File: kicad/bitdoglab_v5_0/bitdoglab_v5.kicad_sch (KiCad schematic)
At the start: 45 parts, among them J1 Conn_01x20_Socket, J10 GND, J11 GND, J12 Conn_01x05_Pin, J13 Conn_01x05_Pin, J14 5x5 Matrix led, J15 GND, J16 GND, J17 GND, J18 GND, J19 JOYSTICK, J2 conector_idc, J3 Conn_01x20_Socket, J4 jumper_mic, J5 Conn_01x05_Pin, J6 Conn_01x05_Pin, J7 GND, J8 GND, J9 GND, Q1 DMG2305UX-13, Q2 BC337, Q3 BC337, SW1 RESET, SW2 Button_A, SW3 Button_B, U1 3.3v_tht, U2 LM1117DT-ADJ, U3 BAT (DIS)CHARGE, U4 1063

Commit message: inicio da sincronizacao do esquematico da versão 5.0
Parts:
- added V_BAT1: JST_EH_B2B-EH-A_1x02_P2.50mm_Vertical, symbol Connector:Screw_Terminal_01x02
- Charge DisCharge1: renamed from U3
- J10: value GND -> 3V3
- J11: value GND -> 5V-VSYS
- J15: value GND -> 0
- J16: value GND -> 1
- J17: value GND -> 2
- J18: value GND -> 3
- J8: value GND -> ANA-IN
- LED RGB1: renamed from D1
- Reg_3V3: renamed from U2; value LM1117DT-ADJ -> 3.3v_smd; footprint Package_TO_SOT_SMD:TO-252-3_TabPin2 -> Package_TO_SOT_SMD:SOT-223
- SW1: value RESET -> Reset
- SW2: value Button_A -> Botão
- U4: value 1063 -> MIC
- renumbered BZ2 to Buzzer1

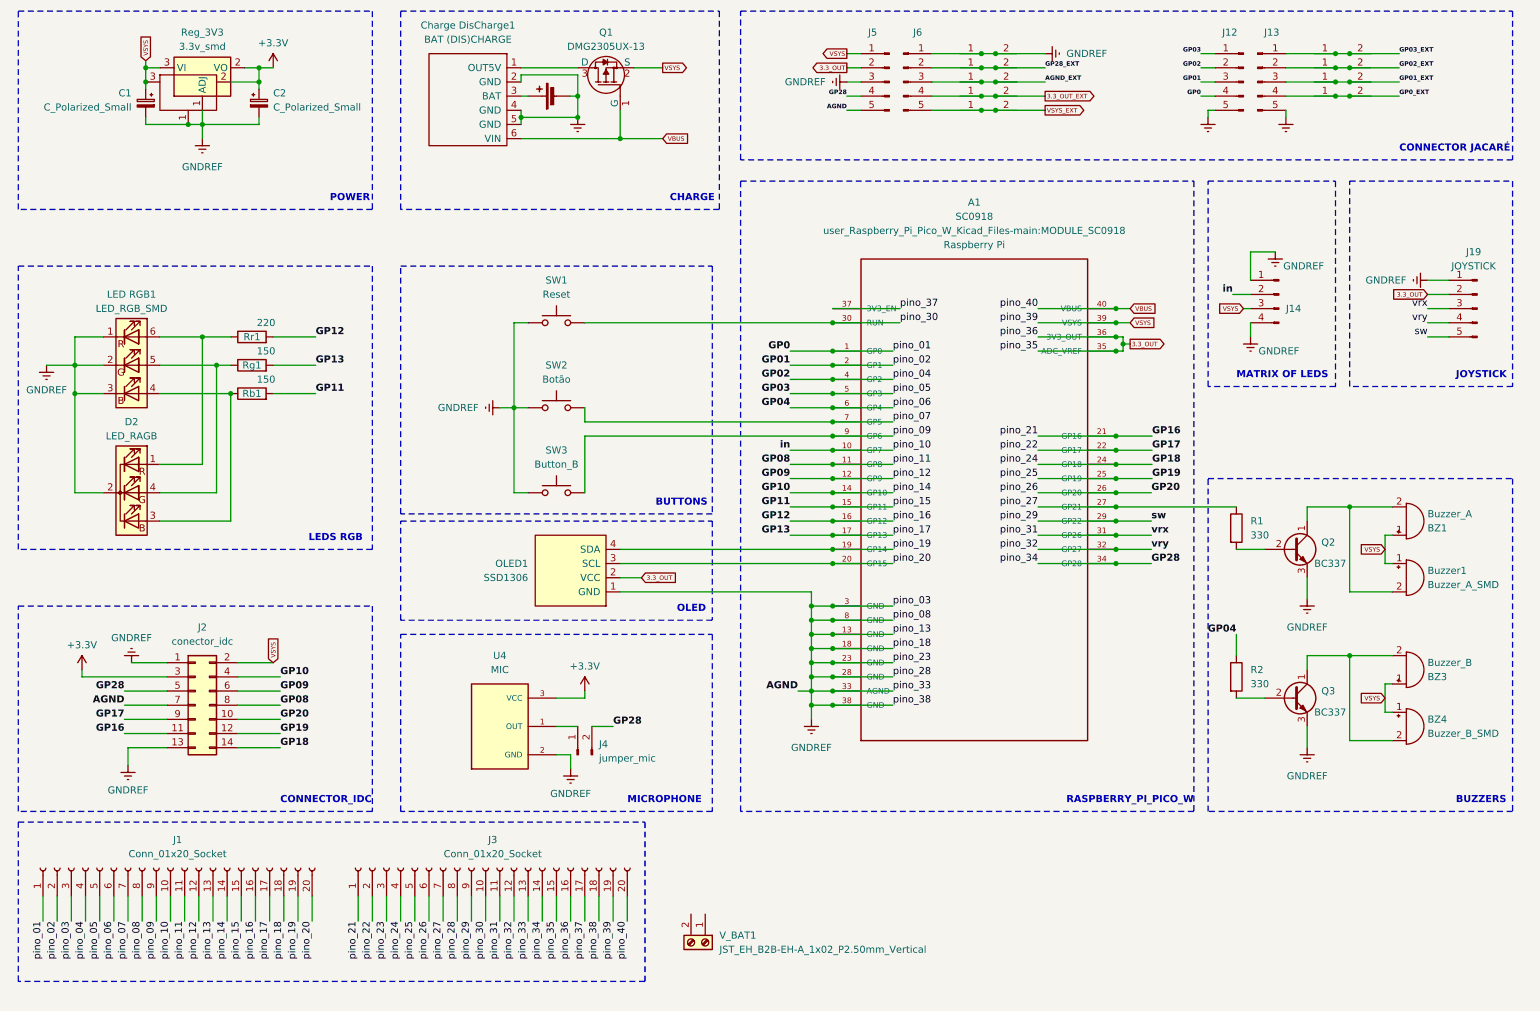
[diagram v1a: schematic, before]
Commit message: Sincronizar layout com esquematico - parte 1
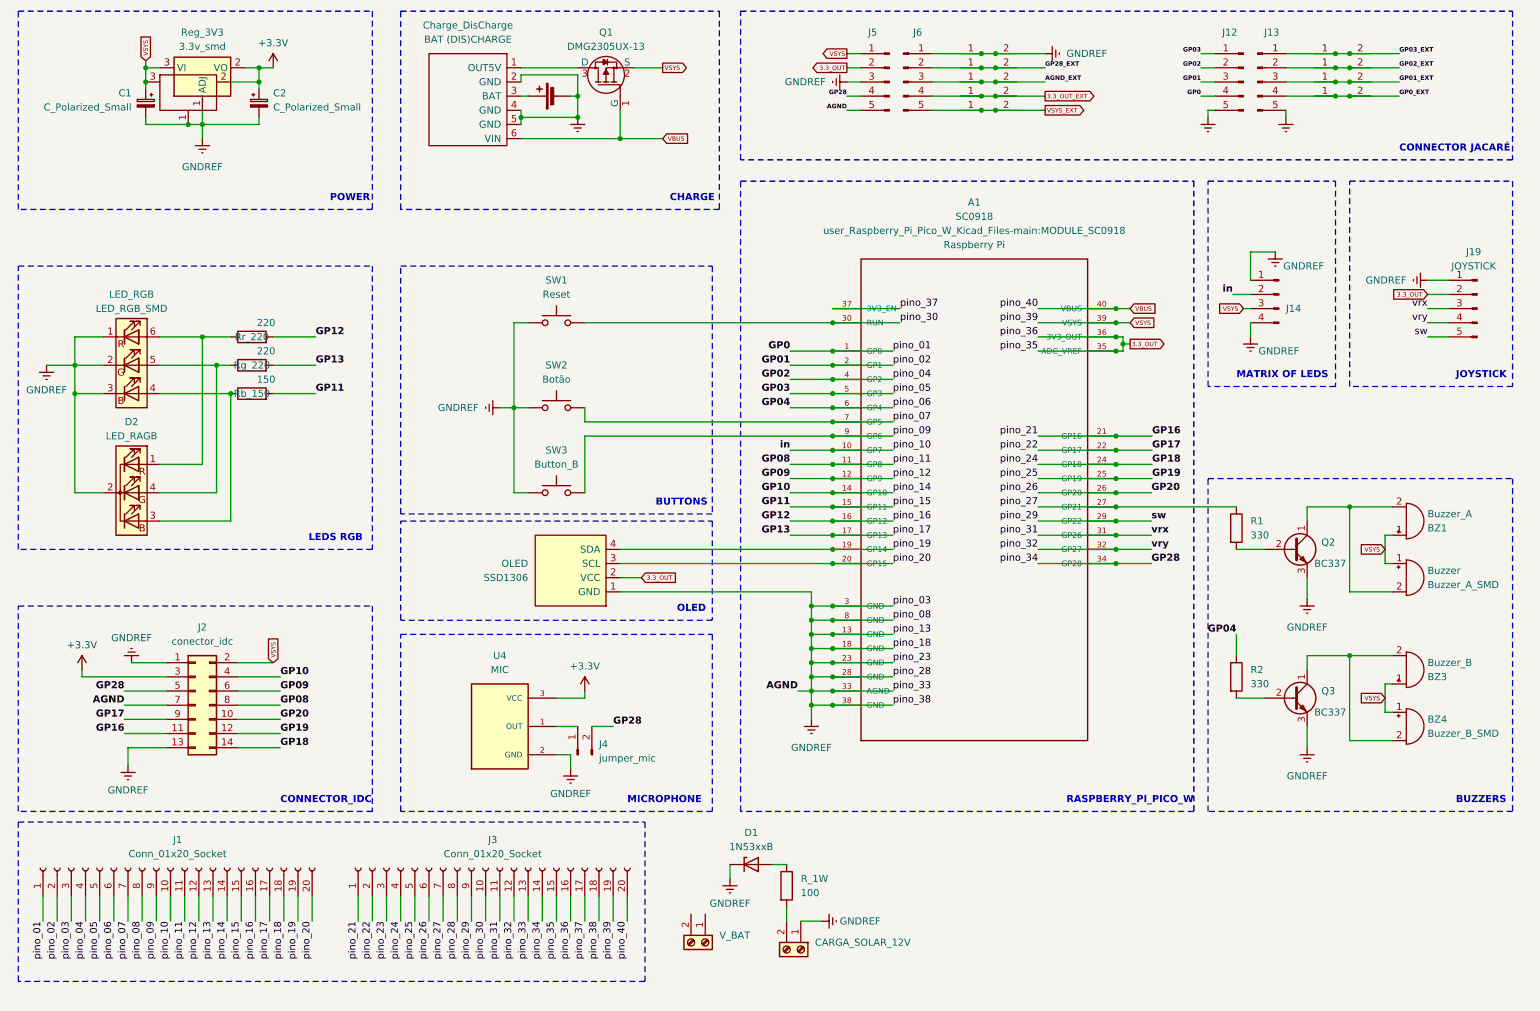
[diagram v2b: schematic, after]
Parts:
- added CARGA_SOLAR_12V: solar, Connector_JST:JST_EH_B2B-EH-A_1x02_P2.50mm_Vertical, symbol Connector:Screw_Terminal_01x02
- added D1: 1N53xxB, Diode_THT:D_DO-201_P15.24mm_Horizontal, symbol Diode:1N53xxB
- added R_1W: 100, Resistor_THT:R_Axial_DIN0411_L9.9mm_D3.6mm_P12.70mm_Horizontal, symbol Device:R
- Charge_DisCharge: renamed from Charge DisCharge1
- LED_RGB: renamed from LED RGB1
- Rg_220: renamed from Rg1; value 150 -> 220
- renumbered Buzzer1 to Buzzer, OLED1 to OLED, Rb1 to Rb_150, Rr1 to Rr_220, V_BAT1 to V_BAT
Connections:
- net GNDREF: now also CARGA_SOLAR_12V.1 (Pin_1), D1.1 (K)
- new net: D1.2 (A), R_1W.1
- new net: CARGA_SOLAR_12V.2 (Pin_2), R_1W.2

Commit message: Sincronizar layout com esquematico - parte 2
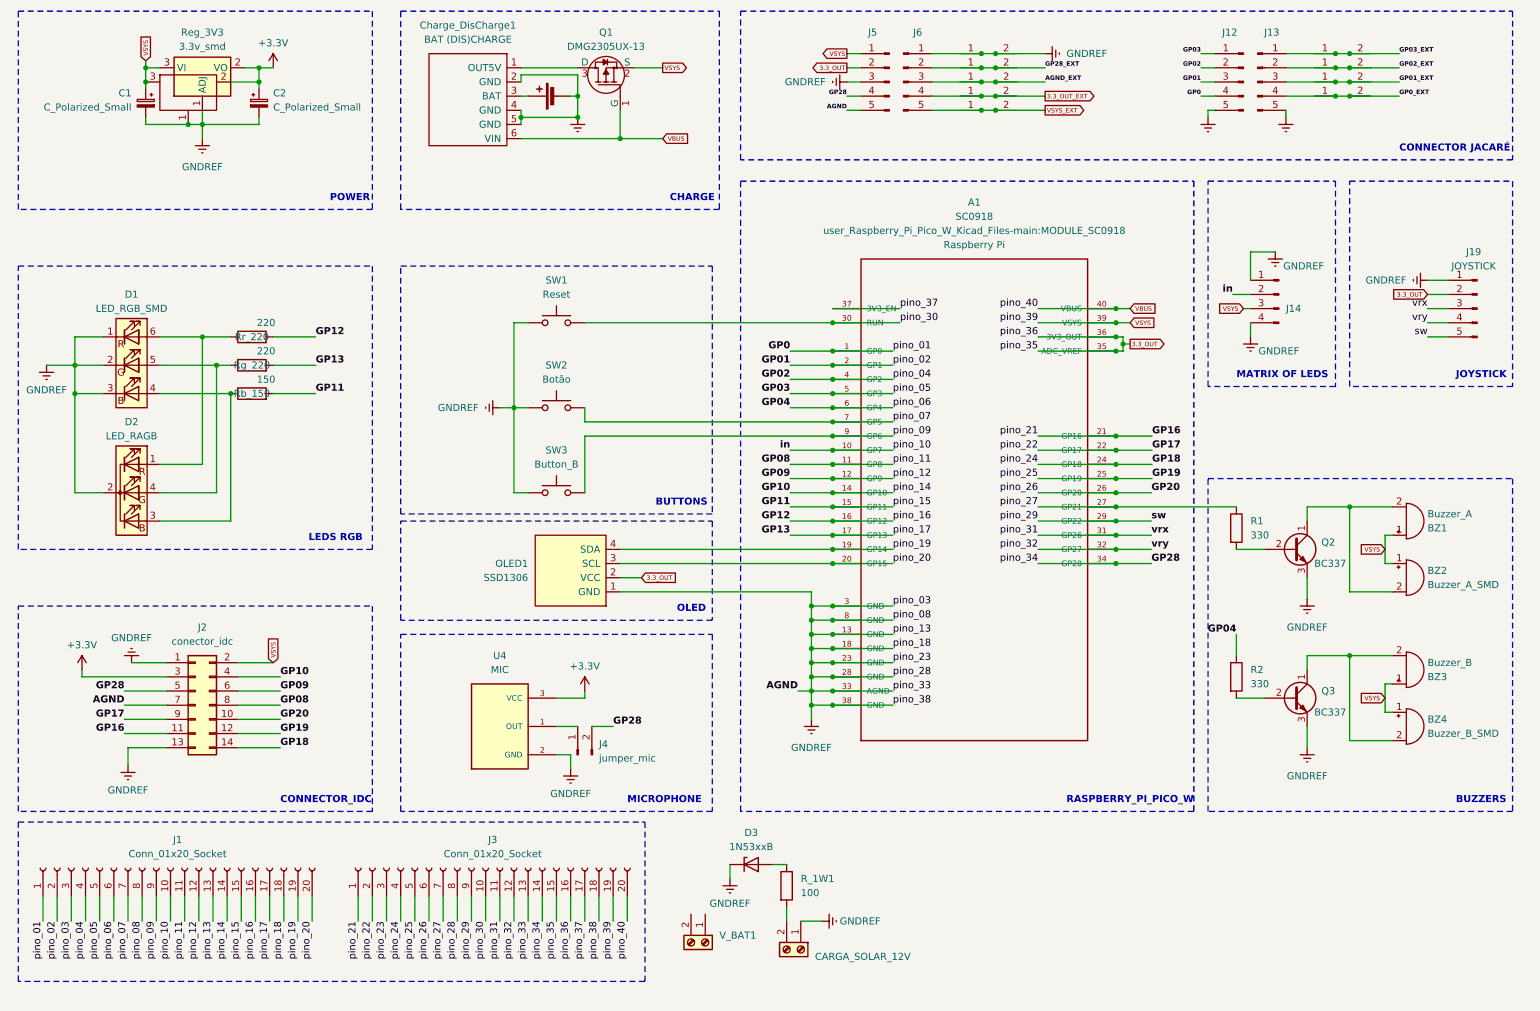
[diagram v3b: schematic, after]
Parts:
- CARGA_SOLAR1: renamed from CARGA_SOLAR_12V; value solar -> CARGA_SOLAR_12V
- V_BAT1: renamed from V_BAT; value JST_EH_B2B-EH-A_1x02_P2.50mm_Vertical -> V_BAT; footprint (none) -> Connector_JST:JST_EH_B2B-EH-A_1x02_P2.50mm_Vertical
- renumbered Buzzer to BZ2, Charge_DisCharge to Charge_DisCharge1, LED_RGB to D1, D1 to D3, OLED to OLED1, R_1W to R_1W1
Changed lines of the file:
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@@
   (symbol (lib_id "Device:Buzzer") (at 264.16 121.92 0) (unit 1)
     (in_bom yes) (on_board yes) (dnp no) (fields_autoplaced)
-    (property "Reference" "Buzzer" (at 267.97 120.65 0)
+    (property "Reference" "BZ2" (at 267.97 120.65 0)
       (effects (font (size 1.27 1.27)) (justify left))
     )
@@
       (project "bitdoglab_v5"
         (path "/09159d3e-7c55-4754-a166-a35b245d09f3"
-          (reference "Buzzer") (unit 1)
+          (reference "BZ2") (unit 1)
         )
       )
@@
   (symbol (lib_id "Diode:1N53xxB") (at 146.685 173.355 0) (unit 1)
     (in_bom yes) (on_board yes) (dnp no) (fields_autoplaced)
-    (property "Reference" "D1" (at 146.685 167.64 0)
+    (property "Reference" "D3" (at 146.685 167.64 0)
       (effects (font (size 1.27 1.27)))
     )
@@
       (project "bitdoglab_v5"
         (path "/09159d3e-7c55-4754-a166-a35b245d09f3"
-          (reference "D1") (unit 1)
+          (reference "D3") (unit 1)
         )
       )
@@
   (symbol (lib_id "Connector:Screw_Terminal_01x02") (at 138.43 187.325 270) (unit 1)
     (in_bom yes) (on_board yes) (dnp no) (fields_autoplaced)
-    (property "Reference" "V_BAT" (at 140.97 186.055 90)
-      (effects (font (size 1.27 1.27)) (justify left))
-    )
-    (property "Value" "JST_EH_B2B-EH-A_1x02_P2.50mm_Vertical" (at 140.97 188.595 90)
-      (effects (font (size 1.27 1.27)) (justify left) hide)
-    )
-    (property "Footprint" "" (at 138.43 187.325 0)
+    (property "Reference" "V_BAT1" (at 140.97 186.055 90)
+      (effects (font (size 1.27 1.27)) (justify left))
+    )
+    (property "Value" "V_BAT" (at 140.97 188.595 90)
+      (effects (font (size 1.27 1.27)) (justify left) hide)
+    )
+    (property "Footprint" "Connector_JST:JST_EH_B2B-EH-A_1x02_P2.50mm_Vertical" (at 138.43 187.325 0)
       (effects (font (size 1.27 1.27)) hide)
     )
@@
       (project "bitdoglab_v5"
         (path "/09159d3e-7c55-4754-a166-a35b245d09f3"
-          (reference "V_BAT") (unit 1)
+          (reference "V_BAT1") (unit 1)
         )
       )
@@
   (symbol (lib_id "Device:LED_RGB") (at 35.56 83.82 0) (unit 1)
     (in_bom yes) (on_board yes) (dnp no) (fields_autoplaced)
-    (property "Reference" "LED_RGB" (at 35.56 71.12 0)
+    (property "Reference" "D1" (at 35.56 71.12 0)
       (effects (font (size 1.27 1.27)))
     )
@@
       (project "bitdoglab_v5"
         (path "/09159d3e-7c55-4754-a166-a35b245d09f3"
-          (reference "LED_RGB") (unit 1)
+          (reference "D1") (unit 1)
         )
       )
@@
   (symbol (lib_id "Device:R") (at 153.035 177.165 0) (unit 1)
     (in_bom yes) (on_board yes) (dnp no) (fields_autoplaced)
-    (property "Reference" "R_1W" (at 155.575 175.895 0)
+    (property "Reference" "R_1W1" (at 155.575 175.895 0)
       (effects (font (size 1.27 1.27)) (justify left))
     )
@@
       (project "bitdoglab_v5"
         (path "/09159d3e-7c55-4754-a166-a35b245d09f3"
-          (reference "R_1W") (unit 1)
+          (reference "R_1W1") (unit 1)
         )
       )
@@
   (symbol (lib_id "Connector:Screw_Terminal_01x02") (at 155.575 188.595 270) (unit 1)
     (in_bom yes) (on_board yes) (dnp no) (fields_autoplaced)
-    (property "Reference" "CARGA_SOLAR_12V" (at 158.115 187.325 90)
-      (effects (font (size 1.27 1.27)) (justify left))
-    )
-    (property "Value" "solar" (at 158.115 189.865 90)
-      (effects (font (size 1.27 1.27)) (justify left) hide)
+    (property "Reference" "CARGA_SOLAR1" (at 158.115 187.325 90)
+      (effects (font (size 1.27 1.27)) (justify left) hide)
+    )
+    (property "Value" "CARGA_SOLAR_12V" (at 158.115 189.865 90)
+      (effects (font (size 1.27 1.27)) (justify left))
     )
     (property "Footprint" "Connector_JST:JST_EH_B2B-EH-A_1x02_P2.50mm_Vertical" (at 155.575 188.595 0)
@@
       (project "bitdoglab_v5"
         (path "/09159d3e-7c55-4754-a166-a35b245d09f3"
-          (reference "CARGA_SOLAR_12V") (unit 1)
+          (reference "CARGA_SOLAR1") (unit 1)
         )
       )
@@
   (symbol (lib_id "SSD1306-128x64_OLED:SSD1306") (at 114.3 120.65 270) (mirror x) (unit 1)
     (in_bom yes) (on_board yes) (dnp no)
-    (property "Reference" "OLED" (at 106.68 119.38 90)
+    (property "Reference" "OLED1" (at 106.68 119.38 90)
       (effects (font (size 1.27 1.27)) (justify right))
     )
@@
       (project "bitdoglab_v5"
         (path "/09159d3e-7c55-4754-a166-a35b245d09f3"
-          (reference "OLED") (unit 1)
+          (reference "OLED1") (unit 1)
         )
       )
@@
   (symbol (lib_id "charger2a:Charger2A") (at 88.9 44.45 0) (unit 1)
     (in_bom yes) (on_board yes) (dnp no) (fields_autoplaced)
-    (property "Reference" "Charge_DisCharge" (at 95.885 22.86 0)
+    (property "Reference" "Charge_DisCharge1" (at 95.885 22.86 0)
       (effects (font (size 1.27 1.27)))
     )
@@
       (project "bitdoglab_v5"
         (path "/09159d3e-7c55-4754-a166-a35b245d09f3"
-          (reference "Charge_DisCharge") (unit 1)
-        )
-      )
+          (reference "Charge_DisCharge1") (unit 1)
+        )
+      )

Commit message: Sincronizar layout com esquematico - parte 3
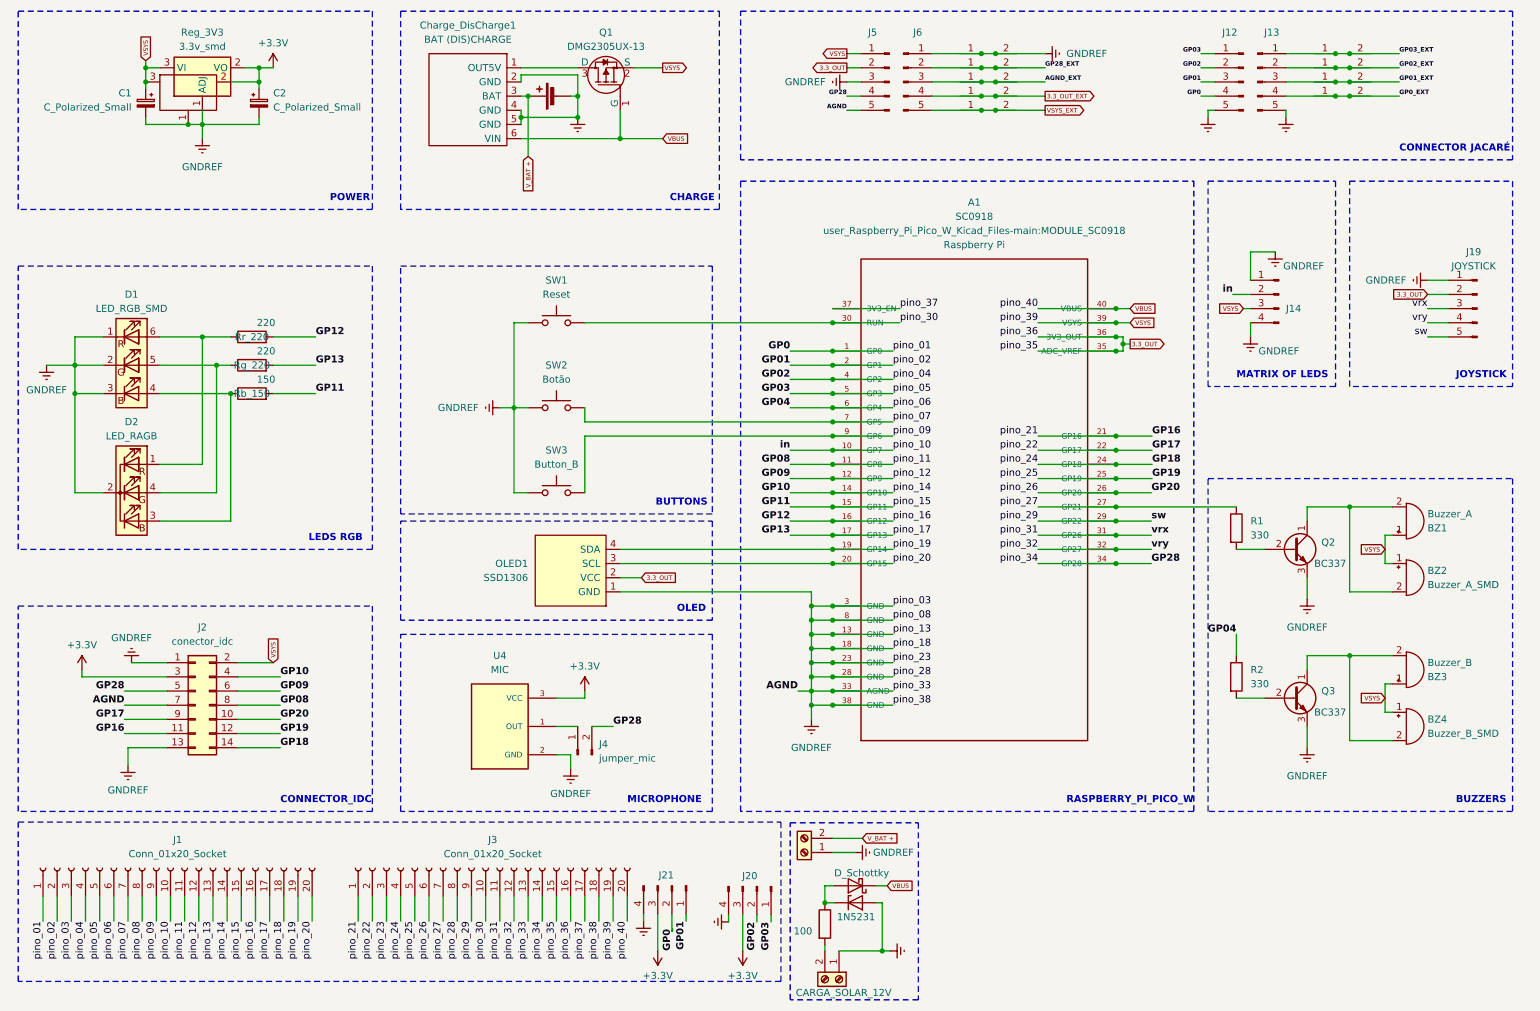
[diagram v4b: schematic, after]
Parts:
- added D4: D_Schottky, Diode_THT:D_DO-15_P3.81mm_Vertical_KathodeUp, symbol Device:D_Schottky
- added J20, J21: Conn_01x04_Pin, Connector_JST:JST_EH_B4B-EH-A_1x04_P2.50mm_Vertical, symbol Connector:Conn_01x04_Pin
- D3: value 1N53xxB -> 1N5231; footprint Diode_THT:D_DO-201_P15.24mm_Horizontal -> Diode_THT:D_T-1_P5.08mm_Horizontal
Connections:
- net +3.3V: now also J20.3 (Pin_3), J21.3 (Pin_3)
- net GNDREF: now also D3.2 (A), V_BAT1.1 (Pin_1), J20.4 (Pin_4), J21.4 (Pin_4); no longer D3.1 (K)
- net GP0: now also J21.2 (Pin_2)
- net GP01: now also J21.1 (Pin_1)
- net GP02: now also J20.2 (Pin_2)
- net GP03: now also J20.1 (Pin_1)
- net VBUS: now also D4.1 (K)
- net at R_1W1.1: now also D3.1 (K), D4.2 (A); no longer D3.2 (A)
- net V_BAT +: now reaches V_BAT1.2 (Pin_2)
- net V_BAT +: now also BT1.1 (+), Charge_DisCharge1.3 (BAT)
